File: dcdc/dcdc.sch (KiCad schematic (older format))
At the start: 46 parts, among them J1 MM3474, J2 Conn_01x05, J3 Conn_01x01, J4 Conn_01x01, J5 Conn_01x01, J6 Conn_01x01, Q1 IRF7403, Q2 IRF7403, Q3 IRF7403, Q4 IRF7403, Q5 IRF7403, Q6 BSS138, Q7 BSS138

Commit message: update readme
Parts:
- removed C1, C10, C11, C2, C5, C6, C7, C9: 0.1uF, symbol Device:C_Small
- removed C3, C4: 1nF, symbol Device:C_Small
- removed C8: 2.2uF, symbol Device:C_Small
- removed D1: D_Small, symbol Device:D_Small
- removed D2: D_Zener_Small, symbol Device:D_Zener_Small
- removed J1: MM3474, Package_SO:SSOP-20_4.4x6.5mm_P0.65mm, symbol Connector_Generic:Conn_02x10_Counter_Clockwise
- removed J2: Conn_01x05, symbol Connector_Generic:Conn_01x05
- removed J3, J4, J5, J6: Conn_01x01, symbol Connector_Generic:Conn_01x01
- removed Q1, Q2, Q3, Q4, Q5: IRF7403, Package_SO:SOIC-8_3.9x4.9mm_P1.27mm, symbol Transistor_FET:IRF7403
- removed Q6, Q7: BSS138, Package_TO_SOT_SMD:SOT-23, symbol Transistor_FET:BSS138
- removed R1, R15, R2, R3, R4, R6: 1k, symbol Device:R_Small
- removed R10: 4.3M, symbol Device:R_Small
- removed R11, R13: 2.2k, symbol Device:R_Small
- removed R12: 10M, symbol Device:R_Small
- removed R14: 5m, symbol Device:R_Small
- removed R16, R17: 470k, symbol Device:R_Small
- removed R18, R19, R20, R5, R7, R8: 100R, symbol Device:R_Small
- removed R9: 5.6M, symbol Device:R_Small

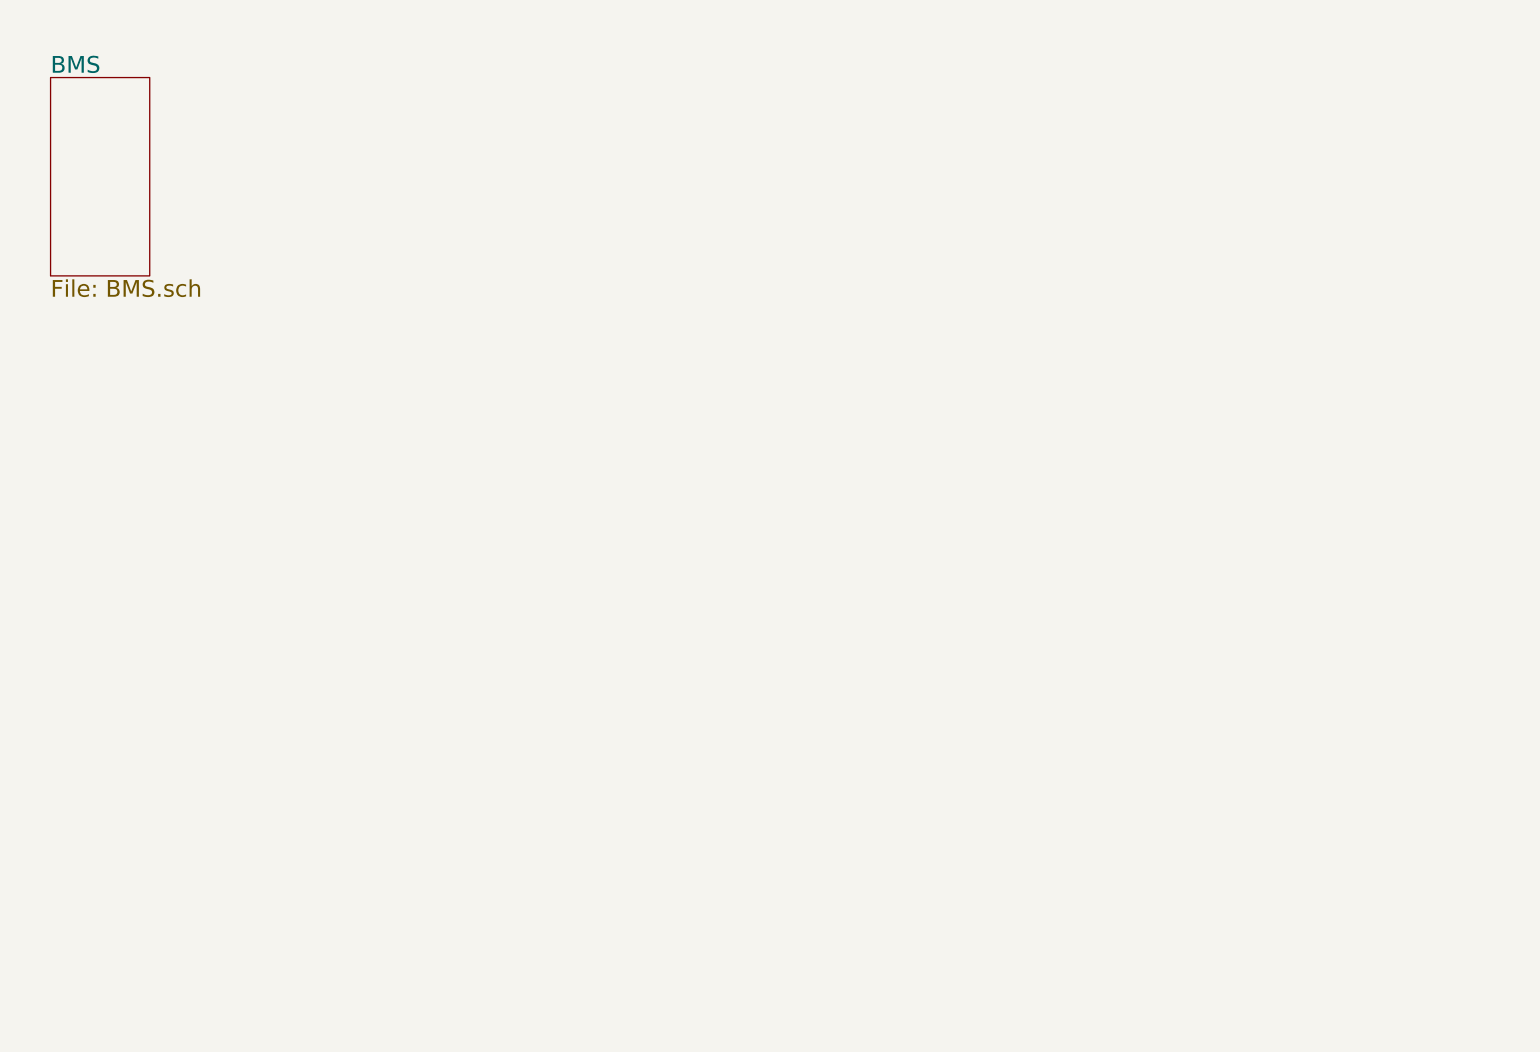
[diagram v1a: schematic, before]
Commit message: update schematic
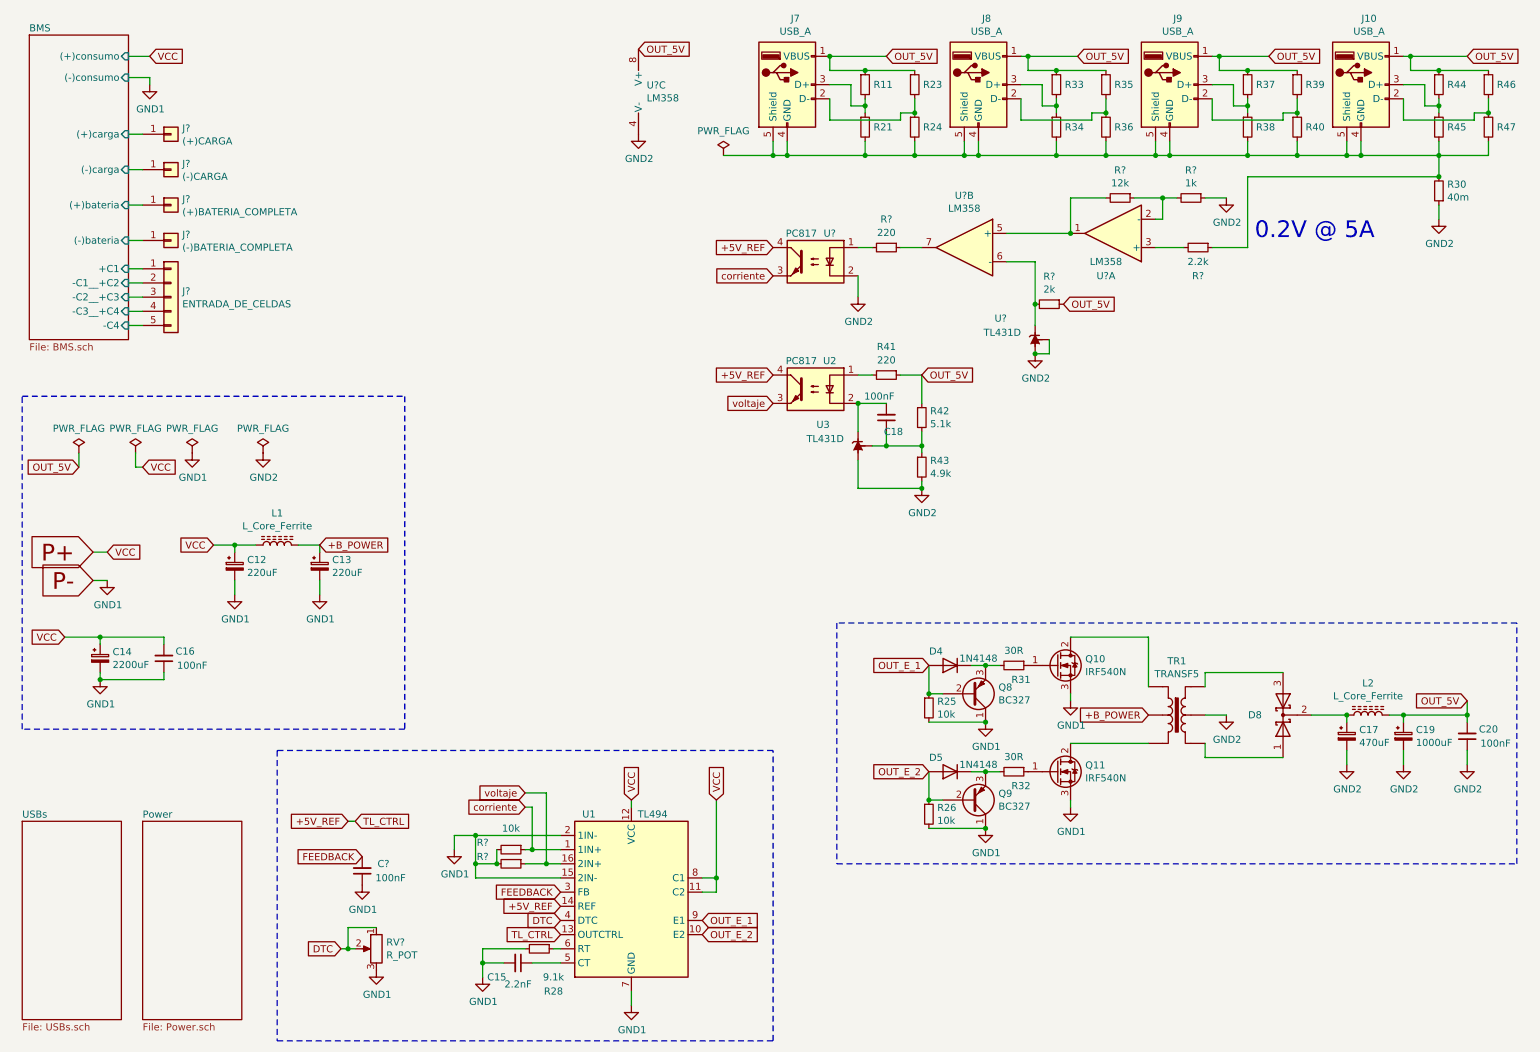
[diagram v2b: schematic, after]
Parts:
- added C12, C13: 220uF, symbol Device:CP_Small
- added C14: 2200uF, symbol Device:CP_Small
- added C15: 2.2nF, symbol Device:C_Small
- added C16, C18, C20, C?: 100nF, symbol Device:C_Small
- added C17: 470uF, symbol Device:CP_Small
- added C19: 1000uF, symbol Device:CP_Small
- added D4, D5: 1N4148, Diode_THT:D_DO-35_SOD27_P7.62mm_Horizontal, symbol Diode:1N4148
- added D8: D_Schottky_x2_KCom_AKA, symbol Device:D_Schottky_x2_KCom_AKA
- added J10, J7, J8, J9: USB_A, symbol Connector:USB_A
- added J?: (+)CARGA, symbol Connector_Generic:Conn_01x01
- added J?: (-)BATERIA_COMPLETA, symbol Connector_Generic:Conn_01x01
- added J?: (-)CARGA, symbol Connector_Generic:Conn_01x01
- added J?: (+)BATERIA_COMPLETA, symbol Connector_Generic:Conn_01x01
- added J?: ENTRADA_DE_CELDAS, symbol Connector_Generic:Conn_01x05
- added L1, L2: L_Core_Ferrite, symbol Device:L_Core_Ferrite
- added Q10, Q11: IRF540N, Package_TO_SOT_THT:TO-220-3_Vertical, symbol Transistor_FET:IRF540N
- added Q8, Q9: BC327, Package_TO_SOT_THT:TO-92_Inline, symbol Transistor_BJT:BC327
- added R11, R21, R23, R24, R33, R34, R35, R36, R37, R38, R39, R40, R44, R45, R46, R47: R, symbol Device:R_Small
- added R25, R26, R? (x2): 10k, symbol Device:R_Small
- added R28: 9.1k, symbol Device:R_Small
- added R30: 40m, symbol Device:R_Small
- added R31, R32: 30R, symbol Device:R_Small
- added R41, R?: 220, symbol Device:R_Small
- added R42: 5.1k, symbol Device:R_Small
- added R43: 4.9k, symbol Device:R_Small
- added R?: 2.2k, symbol Device:R_Small
- added R?: 12k, symbol Device:R_Small
- added R?: 1k, symbol Device:R_Small
- added R?: 2k, symbol Device:R_Small
- added RV?: R_POT, symbol Device:R_POT
- added TR1: TRANSF5, symbol Transformer:TRANSF5
- added U1: TL494, symbol Regulator_Controller:TL494
- added U2, U?: PC817, Package_DIP:DIP-4_W7.62mm, symbol Isolator:PC817
- added U3, U?: TL431D, Package_TO_SOT_THT:TO-92L_Wide, symbol Reference_Voltage:TL431D
- added U? (x3): LM358, symbol Amplifier_Operational:LM358
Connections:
- new net: C15.1, U1.5 (CT)
- new net: R28.1, U1.6 (RT)
- new net: R41.2, U2.1
- new net: C18.2, U2.2, U3.1 (K)
- new net: C18.1, R42.2, R43.1, U3.8 (REF)
- new net: J7.2 (D-), R23.2, R24.1
- new net: J7.3 (D+), R11.2, R21.1
- new net: J10.4 (GND), J10.5 (Shield), J7.4 (GND), J7.5 (Shield), J8.4 (GND), J8.5 (Shield), J9.4 (GND), J9.5 (Shield), R21.2, R24.2, R30.2, R34.2, R36.2, R38.2, R40.2, R45.2, R47.2, R?.1
- new net: J8.2 (D-), R35.2, R36.1
- new net: J8.3 (D+), R33.2, R34.1
- new net: J9.2 (D-), R39.2, R40.1
- new net: J9.3 (D+), R37.2, R38.1
- new net: J10.2 (D-), R46.2, R47.1
- new net: J10.3 (D+), R44.2, R45.1
- new net: D5.1 (K), Q9.3 (E), R32.2
- new net: Q11.1 (G), R32.1
- new net: D4.1 (K), Q8.3 (E), R31.2
- new net: Q10.1 (G), R31.1
- new net: Q10.2 (D), TR1.1
- new net: Q11.2 (D), TR1.3
- new net: D8.1 (A), TR1.4
- new net: D8.3 (A), TR1.6
- new net: C17.1, D8.2 (K), L2.1
- new net: R?.2, U?.1, U?.5 (+)
- new net: R?.1, R?.2, U?.2 (-)
- new net: R?.2, U?.3 (+)
- new net: R?.2, U?.1 (K), U?.6 (-)
- new net: R?.1, U?.7
- new net: R?.2, U?.1
- new net +5V_REF: U1.13 (OUTCTRL), U1.14 (REF), U2.4, U?.4
- new net +B_POWER: C13.1, L1.2, TR1.2
- new net BMS/(+)bateria: J?.1 (Pin_1)
- new net BMS/(+)carga: J?.1 (Pin_1)
- new net BMS/(-)bateria: J?.1 (Pin_1)
- new net BMS/(-)carga: J?.1 (Pin_1)
- new net BMS/+C1: J?.1 (Pin_1)
- new net BMS/-C1__+C2: J?.2 (Pin_2)
- new net BMS/-C2__+C3: J?.3 (Pin_3)
- new net BMS/-C3__+C4: J?.4 (Pin_4)
- new net BMS/-C4: J?.5 (Pin_5)
- new net DTC: RV?.1, RV?.2, U1.4 (DTC)
- new net FEEDBACK: C?.2, U1.3 (FB)
- new net GND1: C12.2, C13.2, C14.2, C15.2, C16.1, C?.1, Q10.3 (S), Q11.3 (S), Q8.1 (C), Q9.1 (C), R25.2, R26.2, R28.2, R?.2, R?.2, RV?.3, U1.15 (2IN-), U1.2 (1IN-), U1.7 (GND)
- new net GND2: C17.2, C19.2, C20.1, R30.1, R43.2, R?.1, TR1.5, U3.2 (A), U3.3 (A), U3.6 (A), U3.7 (A), U?.2, U?.2 (A), U?.3 (A), U?.4 (V-), U?.6 (A), U?.7 (A), U?.8 (REF)
- new net OUT_5V: C19.1, C20.2, J10.1 (VBUS), J7.1 (VBUS), J8.1 (VBUS), J9.1 (VBUS), L2.2, R11.1, R23.1, R33.1, R35.1, R37.1, R39.1, R41.1, R42.1, R44.1, R46.1, R?.1, U?.8 (V+)
- new net OUT_E_1: D4.2 (A), Q8.2 (B), R25.1, U1.9 (E1)
- new net OUT_E_2: D5.2 (A), Q9.2 (B), R26.1, U1.10 (E2)
- new net P+: C12.1, C14.1, C16.2, L1.1, U1.11 (C2), U1.12 (VCC), U1.8 (C1)
- new net corriente: R?.1, U1.1 (1IN+), U?.3
- new net voltaje: R?.1, U1.16 (2IN+), U2.3
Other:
- note added: "0.2V @ 5A"

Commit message: changes
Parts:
- removed J10, J8, J9: USB_A, symbol Connector:USB_A
- removed R33, R34, R35, R36, R37, R38, R39, R40, R44, R45, R46, R47: R, symbol Device:R_Small
- removed R?: 2.2k, symbol Device:R_Small
- removed R?: 2k, symbol Device:R_Small
- removed U? (x3): LM358, symbol Amplifier_Operational:LM358
- removed U?: TL431D, Package_TO_SOT_THT:TO-92L_Wide, symbol Reference_Voltage:TL431D
- added J? (x3): USB_A, symbol Connector:USB_A
- added Q?: BC548, Package_TO_SOT_THT:TO-92_Inline, symbol Transistor_BJT:BC548
- added R? (x8): 1k, symbol Device:R_Small
- added R?: 100k, symbol Device:R_Small
- added R? (x12): R, symbol Device:R_Small
- added R? (x3): 40m, symbol Device:R_Small
- added R? (x8): 4.7k, symbol Device:R_Small
- added U? (x5): LM339, symbol Comparator:LM339
- R?: value 12k -> 4.7k
- R?: value 1k -> 4.7k
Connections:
- net GND2: now also R?.1, Q?.3 (E), R?.1, R?.1, R?.1, U?.12 (V-); no longer R?.1, U?.2
- net OUT_5V: now also R?.1, R?.2, J?.1 (VBUS), J?.1 (VBUS), J?.1 (VBUS), R?.1, R?.1, R?.1, R?.1, R?.1, R?.1, R?.1, R?.2, R?.2, R?.2, U?.3 (V+)
- net at J7.4 (GND), J7.5 (Shield), R21.2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: now also R?.1
- net REF_C: now reaches R?.2
- net REF_C: now also R?.1, R?.1, R?.1, R?.1, R?.2
- new net: Q?.1 (C), U?.2
- new net: R?.2, U?.4 (-)
- new net: R?.2, U?.5 (+)
- new net: J?.2 (D-), R?.1, R?.2 (x3)
- new net: J?.3 (D+), R?.1, R?.2 (x3)
- new net: J?.4 (GND), J?.5 (Shield), R?.1, R?.2, R?.2, R?.2 (x3)
- new net: R?.2, U?.6 (-)
- new net: R?.2, U?.7 (+)
- new net: R?.2, U?.10 (-)
- new net: R?.2, U?.11 (+)
- new net: R?.2, U?.8 (-)
- new net: R?.2, U?.9 (+)
- new net: R?.1, R?.1, R?.1, R?.1, R?.1
- new net: Q?.2 (B), R?.2
- new net OUT_COMP_1: R?.1, R?.2, U?.2
- new net OUT_COMP_2: R?.1, R?.2, U?.1
- new net OUT_COMP_3: R?.1, R?.2, U?.13
- new net OUT_COMP_4: R?.1, R?.2, U?.14
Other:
- note removed: "0.2V @ 5A"
- moved on the sheet: C18, J7, R11, R21, R23, R24, R30, R41, R42, R43, R?, U2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

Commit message: first end
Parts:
- removed C12, C13: 220uF, symbol Device:CP_Small
- removed C14: 2200uF, symbol Device:CP_Small
- removed C17: 470uF, symbol Device:CP_Small
- removed C18, C20: 100nF, symbol Device:C_Small
- removed C19: 1000uF, symbol Device:CP_Small
- removed D4, D5: 1N4148, Diode_THT:D_DO-35_SOD27_P7.62mm_Horizontal, symbol Diode:1N4148
- removed D8: D_Schottky_x2_KCom_AKA, symbol Device:D_Schottky_x2_KCom_AKA
- removed J7, J? (x3): USB_A, symbol Connector:USB_A
- removed L1, L2: L_Core_Ferrite, symbol Device:L_Core_Ferrite
- removed Q10, Q11: IRF540N, Package_TO_SOT_THT:TO-220-3_Vertical, symbol Transistor_FET:IRF540N
- removed Q8, Q9: BC327, Package_TO_SOT_THT:TO-92_Inline, symbol Transistor_BJT:BC327
- removed Q?: BC548, Package_TO_SOT_THT:TO-92_Inline, symbol Transistor_BJT:BC548
- removed R11, R21, R23, R24, R? (x12): R, symbol Device:R_Small
- removed R25, R26: 10k, symbol Device:R_Small
- removed R30, R? (x3): 40m, symbol Device:R_Small
- removed R31, R32: 30R, symbol Device:R_Small
- removed R41, R?: 220, symbol Device:R_Small
- removed R42: 5.1k, symbol Device:R_Small
- removed R43: 4.9k, symbol Device:R_Small
- removed R? (x10): 4.7k, symbol Device:R_Small
- removed R? (x8): 1k, symbol Device:R_Small
- removed R?: 100k, symbol Device:R_Small
- removed TR1: TRANSF5, symbol Transformer:TRANSF5
- removed U2, U?: PC817, Package_DIP:DIP-4_W7.62mm, symbol Isolator:PC817
- removed U3: TL431D, Package_TO_SOT_THT:TO-92L_Wide, symbol Reference_Voltage:TL431D
- removed U? (x5): LM339, symbol Comparator:LM339
- added J11, J13: (+)CONSUMO, Connector_Pin:Pin_D1.0mm_L10.0mm_LooseFit, symbol Connector_Generic:Conn_01x01
- added J12, J14: (-)CONSUMO, Connector_Pin:Pin_D1.0mm_L10.0mm_LooseFit, symbol Connector_Generic:Conn_01x01
- C15: footprint (none) -> Capacitor_THT:C_Disc_D5.0mm_W2.5mm_P2.50mm
- C16: footprint (none) -> Capacitor_THT:C_Rect_L7.2mm_W3.5mm_P5.00mm_FKS2_FKP2_MKS2_MKP2
- C21: renamed from C?; footprint (none) -> Capacitor_THT:C_Rect_L7.2mm_W3.5mm_P5.00mm_FKS2_FKP2_MKS2_MKP2
- J2, J3, J4, J5: renamed from J?; footprint (none) -> Connector_Pin:Pin_D1.0mm_L10.0mm_LooseFit
- J6: renamed from J?; footprint (none) -> Connector_PinHeader_2.54mm:PinHeader_1x05_P2.54mm_Vertical
- R28: footprint (none) -> Resistor_THT:R_Axial_DIN0204_L3.6mm_D1.6mm_P7.62mm_Horizontal
- R29, R33: renamed from R?; footprint (none) -> Resistor_SMD:R_0805_2012Metric_Pad1.20x1.40mm_HandSolder
- RV1: renamed from RV?; footprint (none) -> Potentiometer_THT:Potentiometer_Bourns_3296W_Vertical
- U1: footprint (none) -> Package_DIP:DIP-16_W7.62mm_LongPads
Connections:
- net GND1: now also J14.1 (Pin_1)
- net P+: now also J13.1 (Pin_1)
- new net BMS/(+)consumo: J11.1 (Pin_1)
- new net BMS/(-)consumo: J12.1 (Pin_1)
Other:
- moved on the sheet: C15, C16, C21, J2, J3, J4, J5, J6, R28, R29, R33, RV1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
